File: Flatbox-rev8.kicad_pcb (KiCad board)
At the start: 2 copper layers, 210 x 123.6 mm, 71 parts, among them SW1 SW_Push, SW10 GPIO18, SW11 GPIO25, SW12 GPIO27, SW13 GPIO29, SW14 GPIO19, SW15 GPIO24, SW16 GPIO26, SW17 GPIO28, SW18 GPIO16, SW19 SW_Push, SW2 SW_Push, SW20 SW_Push, SW3 SW_Push, SW4 SW_Push, SW5 SW_Push, SW6 SW_Push, SW7 GPIO9, SW8 GPIO10, SW9 GPIO11, U1 RP2350_60QFN, U2 TLV73333PDBV, U3 W25Q128JVS, Y1 ABM8-272-T3

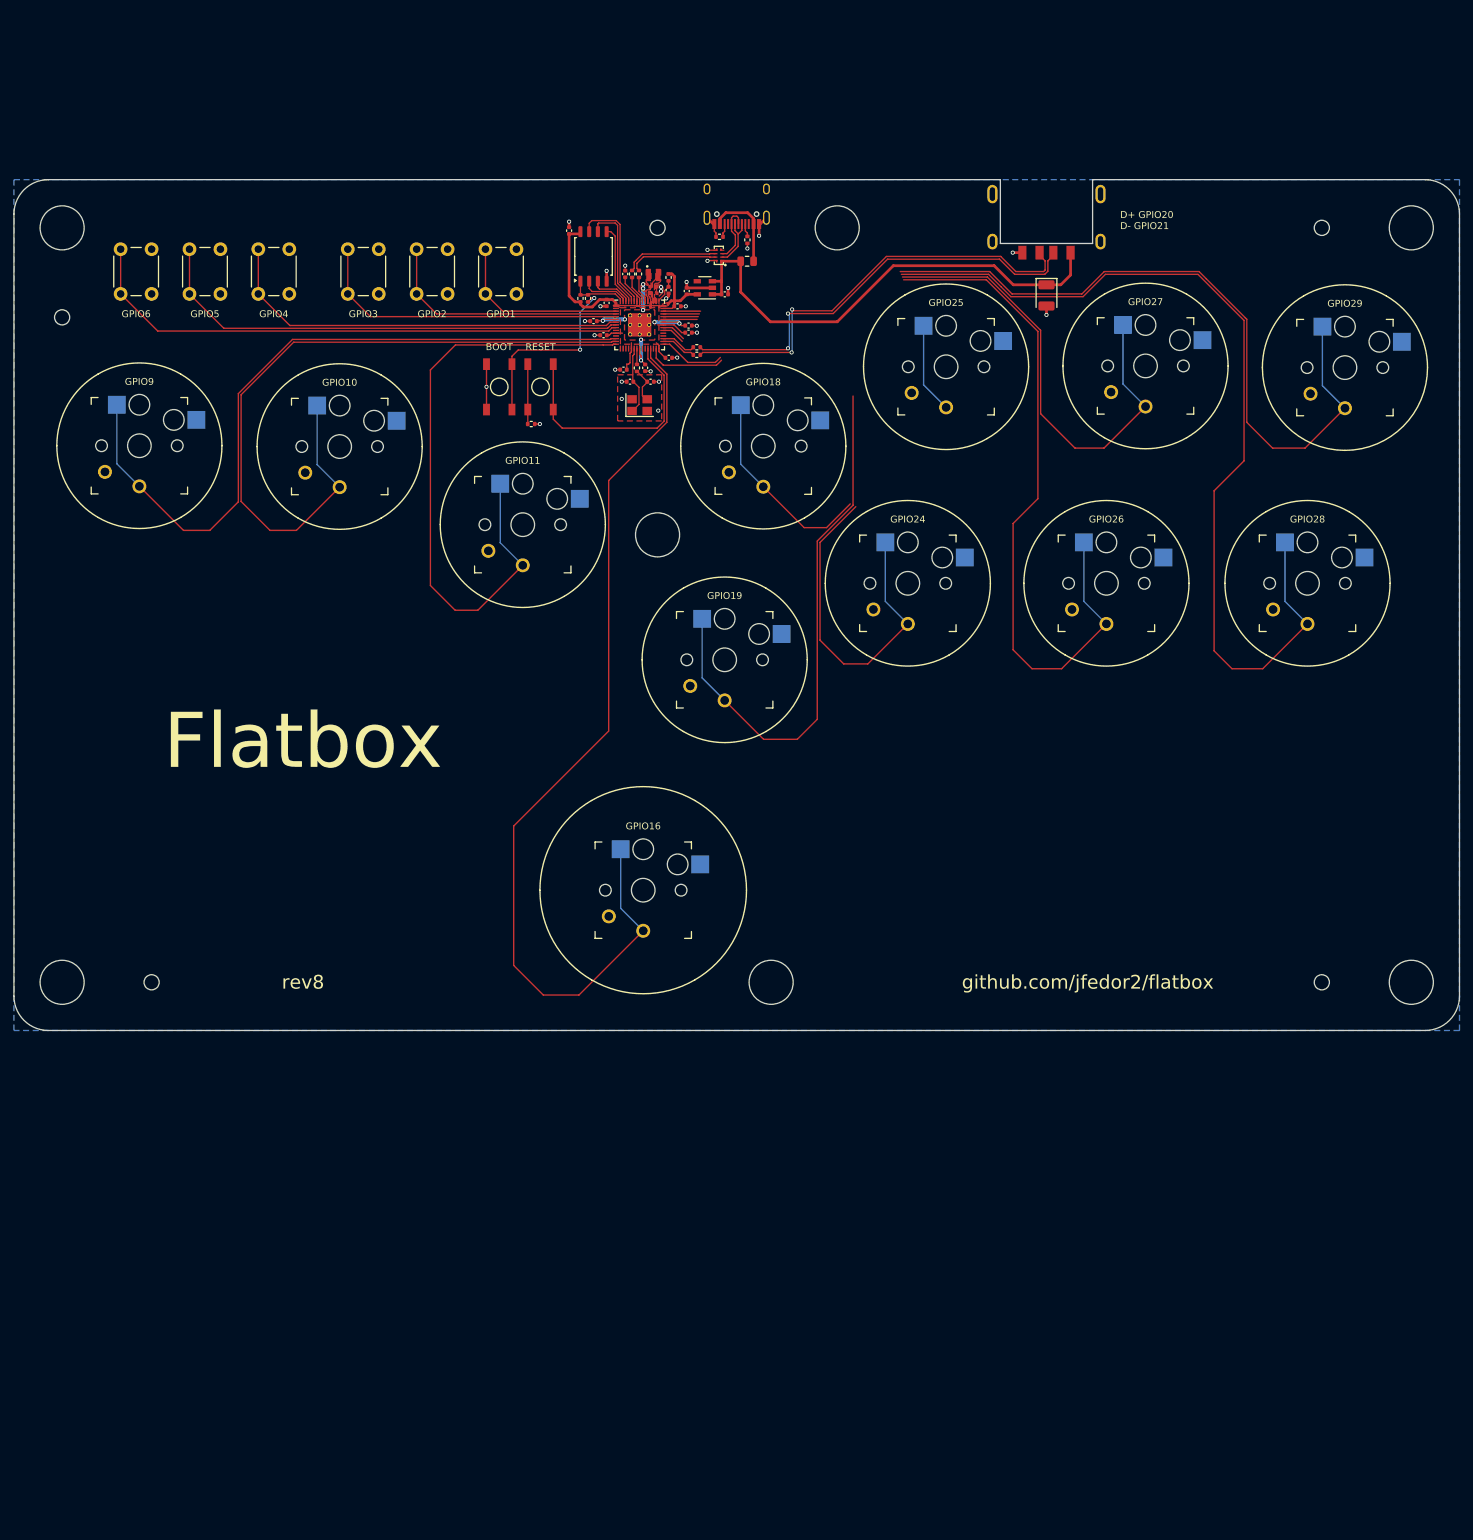
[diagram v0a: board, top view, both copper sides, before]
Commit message: Added pinout for case rgb and switch RGB, moved USB to suitable location
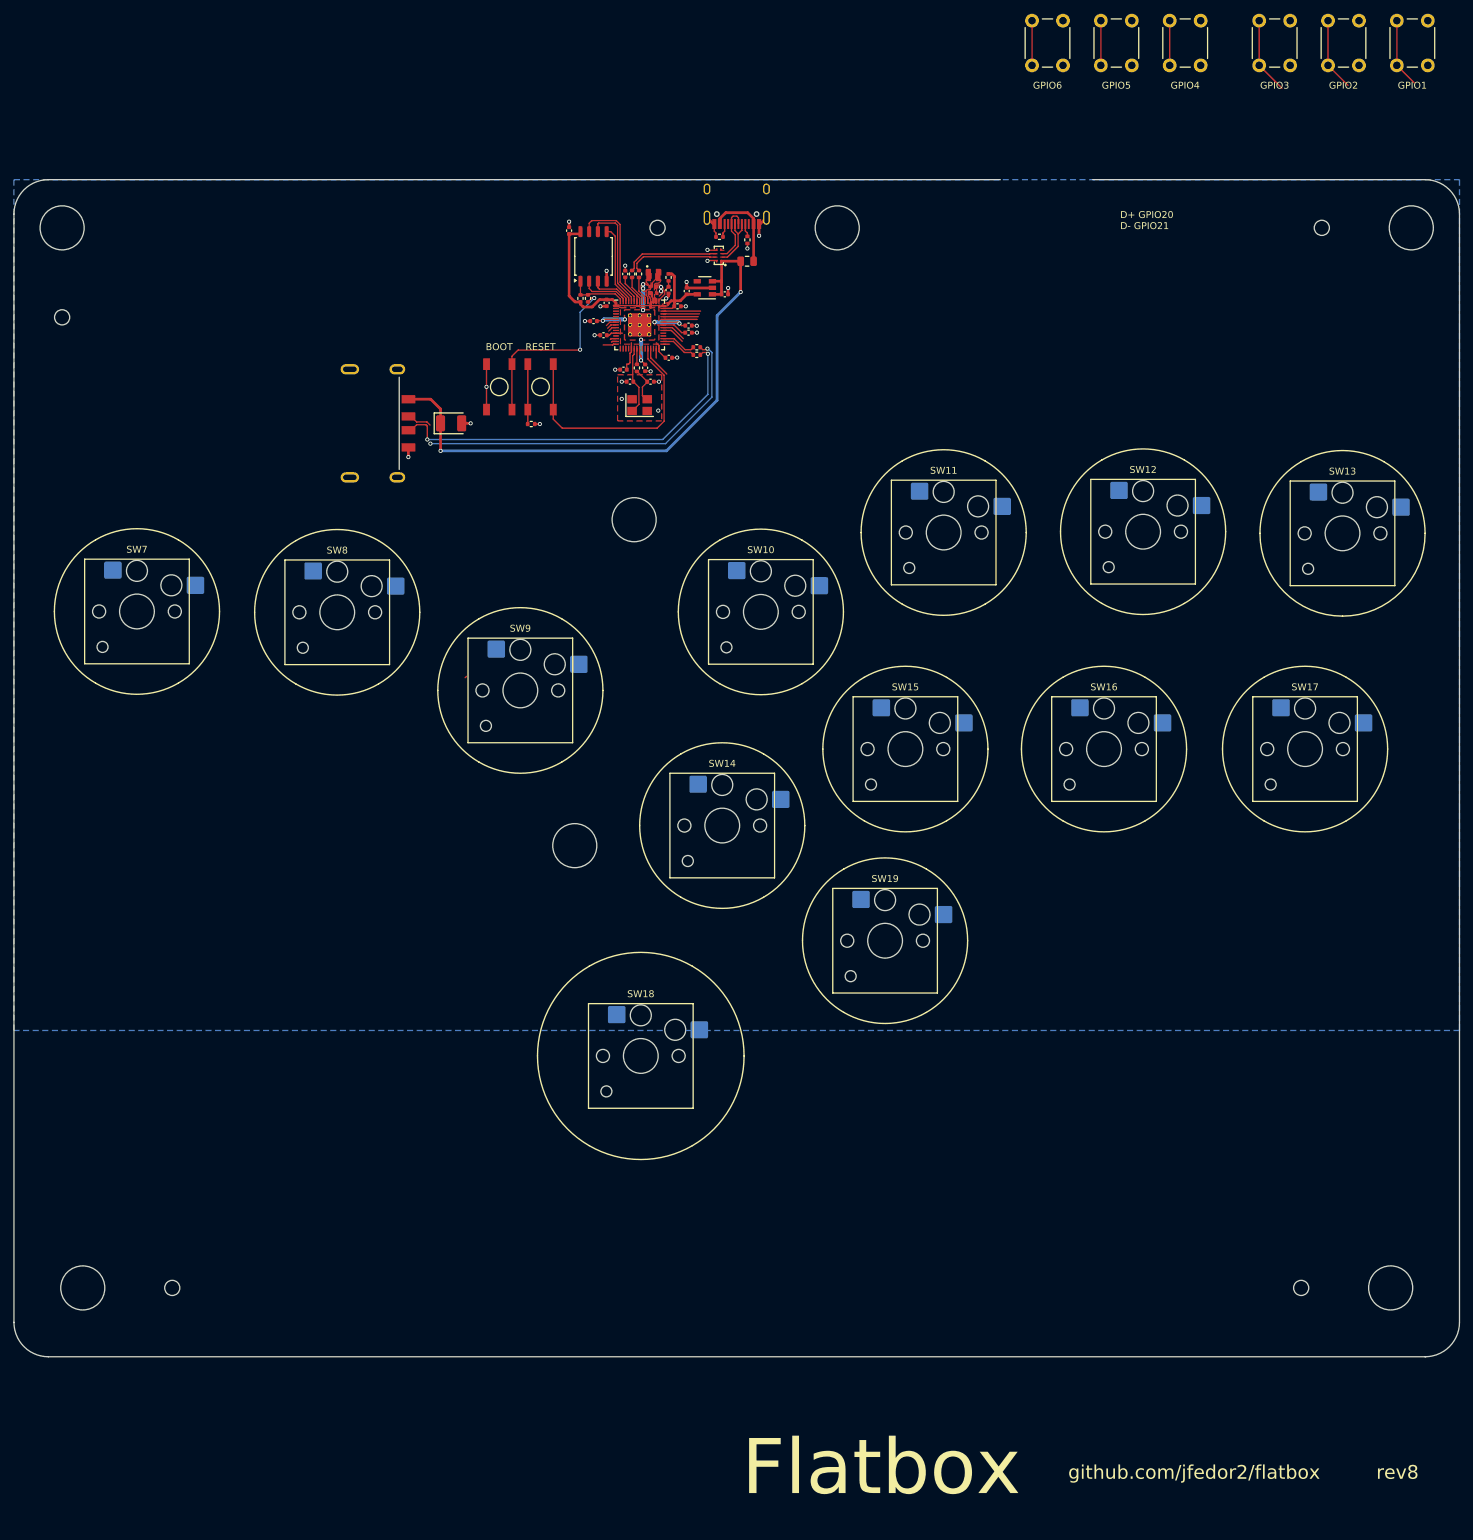
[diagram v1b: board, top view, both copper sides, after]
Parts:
- added SW19: GPIO24, PCM_Switch_Keyboard_Hotswap_Kailh:SW_Hotswap_Kailh_Choc_V1V2, F.Cu at (141.1, 124.6)
- SW10, SW11, SW12, SW13, SW14, SW15, SW16, SW17, SW18, SW7, SW8, SW9: footprint Kailh:Kailh_socket_PG1350_optional -> PCM_Switch_Keyboard_Hotswap_Kailh:SW_Hotswap_Kailh_Choc_V1V2
- moved SW1 136.5 mm to (162.4, -2.60)
- moved SW2 136.5 mm to (172.4, -2.60)
- moved SW3 136.5 mm to (182.4, -2.60)
- moved SW4 136.5 mm to (195.4, -2.60)
- moved SW5 136.5 mm to (205.4, -2.60)
- moved SW6 136.5 mm to (215.4, -2.60)
- moved USB2 101.2 mm to (67.6, 49.4), turned to -90 degrees
- moved C19 88.5 mm to (78.0, 49.4), turned to 0 degrees
- moved H1 44.5 mm to (24.5, 175.0)
- moved H3 44.5 mm to (214.5, 175.0)
- moved H8 44.5 mm to (37.5, 175.0)
- moved H9 44.5 mm to (201.5, 175.0)
- moved H2 34.8 mm to (96.0, 110.8)
- moved SW10 24.1 mm to (123.0, 76.8)
- moved SW11 24.1 mm to (149.6, 65.3)
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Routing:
- net L2: track 140.8 -> 5.24 mm
- net UP: track 137.5 -> 4.67 mm
- net LEFT: track 105.8 -> 0.85 mm
- net DOWN: track 105.0 -> 0.69 mm
- net L1: track 107.7 -> 5.41 mm
- net R2: track 105.9 -> 4.91 mm
- net RIGHT: track 90.6 -> 1.90 mm
- net CROSS: track 89.0 -> 0.91 mm
- net OPT1: track 80.9 -> 7.76 mm
- net R1: track 73.5 -> 5.08 mm
- net OPT2: track 70.7 -> 7.92 mm
- net OPT3: track 60.6 -> 8.09 mm
- net CIRCLE: track 54.8 -> 3.41 mm
- net SQUARE: track 41.3 -> 1.39 mm
- net OPT4: track 46.8 -> 11.2 mm
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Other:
- board size 210 x 123.6 mm -> 210 x 171 mm

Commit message: Redone butotn layout (sort of) and localized general area for booter location
- MAKE NEW FOOTPRINT FOR LED + SWITCH COMBO
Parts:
- added REF**: LED_WS2812B-Mini_PLCC4_3.5x3.5mm, LED_SMD:LED_WS2812B-Mini_PLCC4_3.5x3.5mm, F.Cu at (32.1, 91.7)
- added REF**: LED_WS2812B-Mini_PLCC4_3.5x3.5mm, LED_SMD:LED_WS2812B-Mini_PLCC4_3.5x3.5mm, F.Cu at (160.4, 92.9)
- added REF**: LED_WS2812B-Mini_PLCC4_3.5x3.5mm, LED_SMD:LED_WS2812B-Mini_PLCC4_3.5x3.5mm, F.Cu at (161.6, 64.7)
- added REF**: LED_WS2812B-Mini_PLCC4_3.5x3.5mm, LED_SMD:LED_WS2812B-Mini_PLCC4_3.5x3.5mm, F.Cu at (181.2, 112.9)
- added REF**: LED_WS2812B-Mini_PLCC4_3.5x3.5mm, LED_SMD:LED_WS2812B-Mini_PLCC4_3.5x3.5mm, F.Cu at (105.7, 156.4)
- added REF**: LED_WS2812B-Mini_PLCC4_3.5x3.5mm, LED_SMD:LED_WS2812B-Mini_PLCC4_3.5x3.5mm, F.Cu at (69.3, 64.3)
- added REF**: LED_WS2812B-Mini_PLCC4_3.5x3.5mm, LED_SMD:LED_WS2812B-Mini_PLCC4_3.5x3.5mm, F.Cu at (154.7, 123.9)
- added REF**: LED_WS2812B-Mini_PLCC4_3.5x3.5mm, LED_SMD:LED_WS2812B-Mini_PLCC4_3.5x3.5mm, F.Cu at (210.2, 112.9)
- added REF**: LED_WS2812B-Mini_PLCC4_3.5x3.5mm, LED_SMD:LED_WS2812B-Mini_PLCC4_3.5x3.5mm, F.Cu at (215.9, 81.4)
- added REF**: LED_WS2812B-Mini_PLCC4_3.5x3.5mm, LED_SMD:LED_WS2812B-Mini_PLCC4_3.5x3.5mm, F.Cu at (61.1, 91.7)
- added REF**: LED_WS2812B-Mini_PLCC4_3.5x3.5mm, LED_SMD:LED_WS2812B-Mini_PLCC4_3.5x3.5mm, F.Cu at (87.6, 103.2)
- added REF**: LED_WS2812B-Mini_PLCC4_3.5x3.5mm, LED_SMD:LED_WS2812B-Mini_PLCC4_3.5x3.5mm, F.Cu at (239.7, 118.1)
- added REF**: LED_WS2812B-Mini_PLCC4_3.5x3.5mm, LED_SMD:LED_WS2812B-Mini_PLCC4_3.5x3.5mm, F.Cu at (145.4, 156.7)
- added REF**: LED_WS2812B-Mini_PLCC4_3.5x3.5mm, LED_SMD:LED_WS2812B-Mini_PLCC4_3.5x3.5mm, F.Cu at (244.9, 86.8)
- added REF**: LED_WS2812B-Mini_PLCC4_3.5x3.5mm, LED_SMD:LED_WS2812B-Mini_PLCC4_3.5x3.5mm, F.Cu at (178.1, 140.6)
- added REF**: LED_WS2812B-Mini_PLCC4_3.5x3.5mm, LED_SMD:LED_WS2812B-Mini_PLCC4_3.5x3.5mm, F.Cu at (186.9, 81.4)
- added SW18: GPIO16, PCM_Switch_Keyboard_Hotswap_Kailh:SW_Hotswap_Kailh_Choc_V1V2, F.Cu at (145.2, 151.5)
- added SW19: GPIO24, PCM_Switch_Keyboard_Hotswap_Kailh:SW_Hotswap_Kailh_Choc_V1V2, F.Cu at (161.7, 59.8)
- added SW8: GPIO10, PCM_Switch_Keyboard_Hotswap_Kailh:SW_Hotswap_Kailh_Choc_V1V2, F.Cu at (69.3, 59.7)
- C19, USB2: moved to B.Cu
- moved USB2 121.6 mm to (189.0, 41.9)
- moved C19 100.8 mm to (178.5, 41.9), turned to 180 degrees
- moved H3 62.2 mm to (276.6, 177.4)
- moved H9 62.2 mm to (263.6, 177.4)
- moved H10 59.2 mm to (263.6, 23.4)
- moved H4 59.2 mm to (276.6, 23.4)
- moved SW13 40.5 mm to (244.7, 81.7)
- moved SW17 40.5 mm to (239.2, 113.0)
- moved SW11 38.8 mm to (186.7, 76.4)
- moved SW12 38.8 mm to (215.7, 76.2)
- moved SW15 38.8 mm to (181.2, 107.8)
- moved SW16 38.8 mm to (210.0, 107.8)
- moved SW10 38.8 mm to (160.2, 87.9)
- moved SW14 38.8 mm to (154.5, 118.9)
- moved SW19 38.8 mm to (178.2, 135.7)
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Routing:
- net HD+: track 56.1 -> 22.8 mm
- net +5V: track 86.4 -> 54.1 mm
- net HD-: track 56.0 -> 24.6 mm
- net (no net): vias 0 -> 1
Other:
- board size 210 x 171 mm -> 272.6 x 171 mm
- board text added: "rev1.2"
- board text removed: "Flatbox"
- board text removed: "github.com/jfedor2/flatbox"
- board text removed: "rev8"

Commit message: Signed-off-by: zephyris <zephyris@ad.uwaesports.org>
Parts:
- added REF**: Adafruit_SSD1306, Display:Adafruit_SSD1306, F.Cu at (63.7, 49.0)
- moved H2 14.5 mm to (108.0, 129.0)
- moved REF** 12.7 mm to (161.6, 77.4)
- moved REF** 12.7 mm to (239.7, 130.7)
- moved REF** 12.7 mm to (178.1, 153.3)
- moved SW14 12.7 mm to (154.5, 131.6)
- moved SW15 12.7 mm to (181.2, 120.5)
- moved SW16 12.7 mm to (210.0, 120.5)
- moved SW17 12.7 mm to (239.2, 125.7)
- moved SW18 12.7 mm to (145.2, 164.2)
- moved SW8 12.7 mm to (61.1, 99.7)
- moved SW19 12.7 mm to (161.7, 72.4)
- moved SW8 12.7 mm to (69.3, 72.3)
- moved REF** 12.7 mm to (32.1, 104.3)
- moved REF** 12.7 mm to (160.4, 105.6)
- moved REF** 12.7 mm to (181.2, 125.6)
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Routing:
- net HD+: track 22.8 -> 78.4 mm
- net HD-: track 24.6 -> 77.0 mm
- net +5V: track 54.1 -> 97.4 mm
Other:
- rule pad_to_mask_clearance: 0 -> 0.2

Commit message: Done up switch traces for main directional and command input
Done up switch traces for main directional and command input

Need to redo schematic for LS RS, Up directional chaining and RGB SMD
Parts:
- removed the REF** at (32.1, 104.3)
- removed the REF** at (160.4, 105.6)
- removed the REF** at (161.6, 77.4)
- removed the REF** at (181.2, 125.6)
- removed the REF** at (105.7, 169.1)
- removed the REF** at (69.3, 77.0)
- removed the REF** at (154.7, 136.6)
- removed the REF** at (210.2, 125.6)
- removed the REF** at (215.9, 94.1)
- removed the REF** at (61.1, 104.3)
- removed the REF** at (87.6, 115.8)
- removed the REF** at (239.7, 130.7)
- removed the REF** at (145.4, 169.3)
- removed the REF** at (244.9, 99.5)
- removed the REF** at (178.1, 153.3)
- removed the REF** at (186.9, 94.1)
- SW10, SW11, SW12, SW13, SW14, SW15, SW16, SW17, SW18 (x2), SW19 (x2), SW7, SW8 (x2), SW9: footprint PCM_Switch_Keyboard_Hotswap_Kailh:SW_Hotswap_Kailh_Choc_V1V2 -> Kailh:Kailh_socket_PG1350_optional
- moved H10 43.0 mm to (301.4, 43.9)
- moved H3 43.0 mm to (314.4, 197.9)
- moved H4 43.0 mm to (314.4, 43.9)
- moved H9 43.0 mm to (301.4, 197.9)
- moved SW5 43.0 mm to (258.5, 47.2)
- moved SW6 43.0 mm to (268.5, 47.2)
- moved C1 43.0 mm to (137.6, 57.5)
- moved C11 43.0 mm to (148.5, 53.0)
- moved C17 43.0 mm to (145.9, 66.3)
- moved C19 43.0 mm to (216.3, 62.4)
- moved C2 43.0 mm to (145.1, 64.2)
- moved C5 43.0 mm to (139.5, 54.8)
- moved F1 43.0 mm to (159.9, 48.8)
- moved H2 43.0 mm to (145.8, 149.5)
- moved H5 43.0 mm to (173.0, 43.9)
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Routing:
- net L2: track 5.24 -> 203.5 mm
- net CROSS: track 0.91 -> 189.5 mm
- net CIRCLE: track 3.41 -> 188.5 mm
- net R1: track 5.08 -> 188.9 mm
- net R2: track 4.91 -> 182.7 mm
- net L1: track 5.41 -> 176.5 mm, vias 0 -> 1
- net TRIANGLE: track 3.58 -> 135.4 mm
- net SQUARE: track 1.39 -> 129.6 mm
- net DOWN: track 0.69 -> 123.0 mm
- net RIGHT: track 1.90 -> 118.7 mm
- net LEFT: track 0.85 -> 115.8 mm
- net UP: track 4.67 -> 31.1 mm
- net OPT6: track 10.0 -> 35.4 mm, vias 0 -> 1
- net OPT5: track 10.6 -> 35.3 mm, vias 0 -> 1
- net OPT4: track 11.2 -> 35.8 mm, vias 0 -> 1
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
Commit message: redone socket, adding RGB lighting and pathing
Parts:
- added REF**: LED_SK6812_EC15_1.5x1.5mm, LED_SMD:LED_SK6812_EC15_1.5x1.5mm, F.Cu at (116.6, 92.8)
- added REF**: LED_SK6812_EC15_1.5x1.5mm, LED_SMD:LED_SK6812_EC15_1.5x1.5mm, F.Cu at (97.6, 92.8)
- SW10, SW11, SW12, SW13, SW14, SW15, SW16, SW17, SW18 (x2), SW19 (x2), SW7, SW8 (x2), SW9: footprint Kailh:Kailh_socket_PG1350_optional -> key-switches:SW_MX_Kailh_Choc_V1V2_HotSwap_Hybrid
- moved C7 4.99 mm to (134.1, 59.5)
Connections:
- U1 pad 12: unconnected-(U1-GPIO8-Pad12) -> RGB
- U1 pad 16: unconnected-(U1-GPIO12-Pad16) -> SCL
- U1 pad 17: unconnected-(U1-GPIO13-Pad17) -> SDA
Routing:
- net LEFT: track 115.8 -> 87.0 mm
- net DOWN: track 123.0 -> 96.4 mm
- net CROSS: track 189.5 -> 164.9 mm
- net R2: track 182.7 -> 165.4 mm
- net TRIANGLE: track 135.4 -> 121.4 mm
- net CIRCLE: track 188.5 -> 175.2 mm
- net UP: track 31.1 -> 17.9 mm
- net SQUARE: track 129.6 -> 116.8 mm
- net L2: track 203.5 -> 190.8 mm
- net RIGHT: track 118.7 -> 106.6 mm
- net +3V3: track 52.6 -> 57.6 mm
